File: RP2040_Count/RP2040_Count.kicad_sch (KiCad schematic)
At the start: 17 parts, among them J2 String1, J3 OLED, SW1 Test, U2 AMS1117-5.0, U4 74AHCT1G125, U4 INA219BxD, U5 RP2040-Tiny

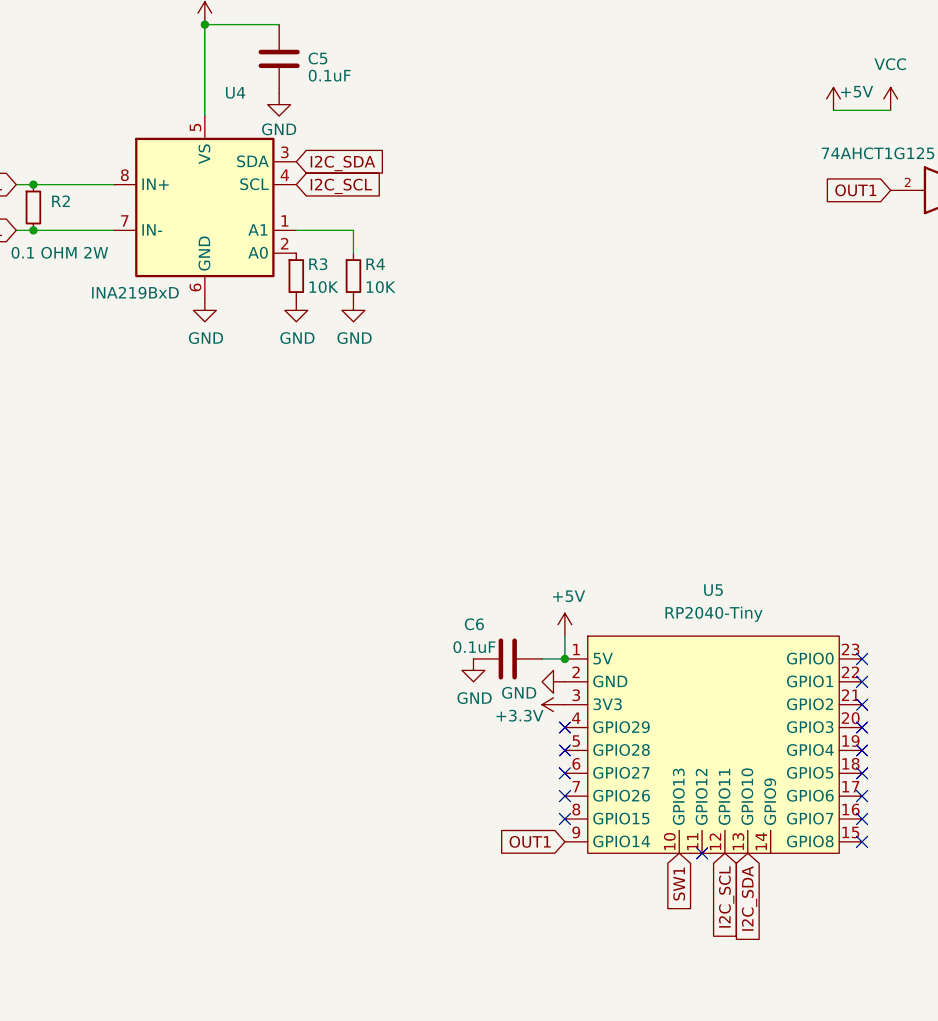
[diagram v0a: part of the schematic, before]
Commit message: add plug in 3 to 4 adapter
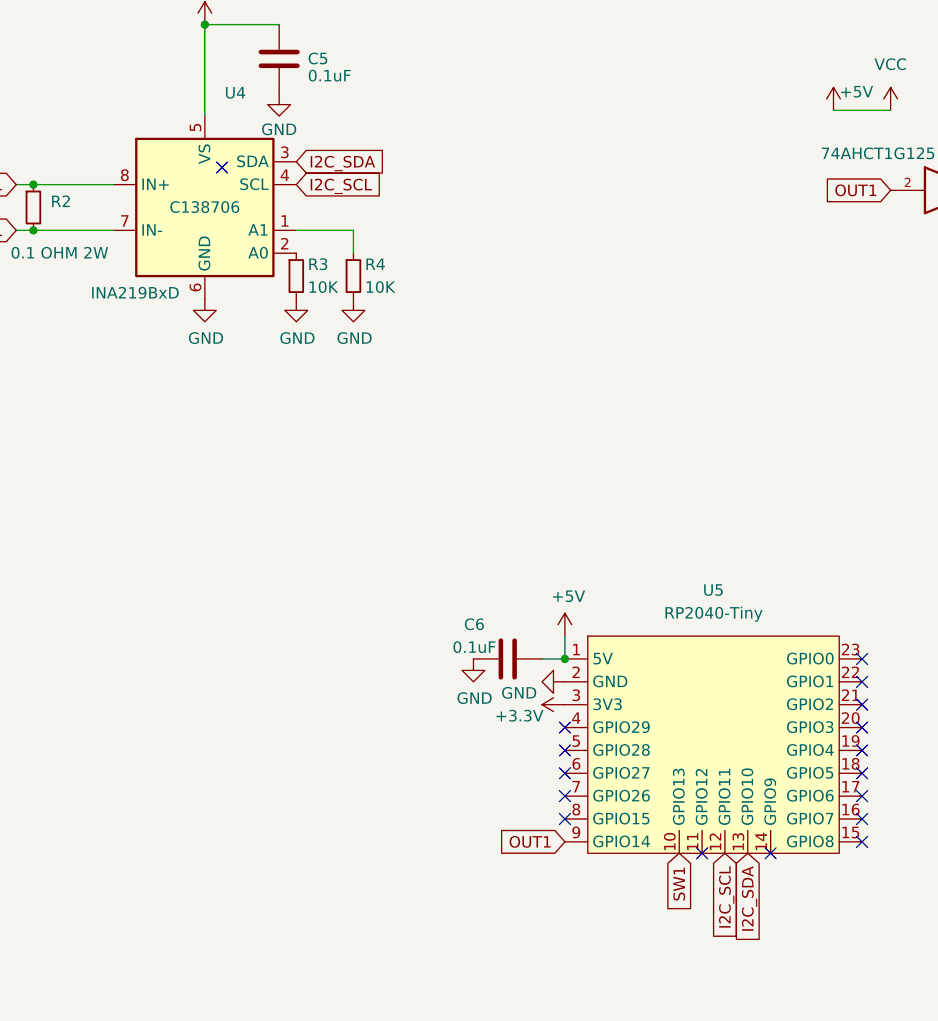
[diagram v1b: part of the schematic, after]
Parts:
- J3: footprint Scotts:OLED-SSD1306-128X64-I2C-THT_2HOLE -> Scotts:OLED-SSD1306-128X64-I2C-THT_SCOTT2
- U4: LCSC (none) -> C138706; LCSC PN C87469 -> C138706
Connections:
- no-connect marks 15 -> 17
